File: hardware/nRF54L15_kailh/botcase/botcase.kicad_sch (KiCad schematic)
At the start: 144 parts

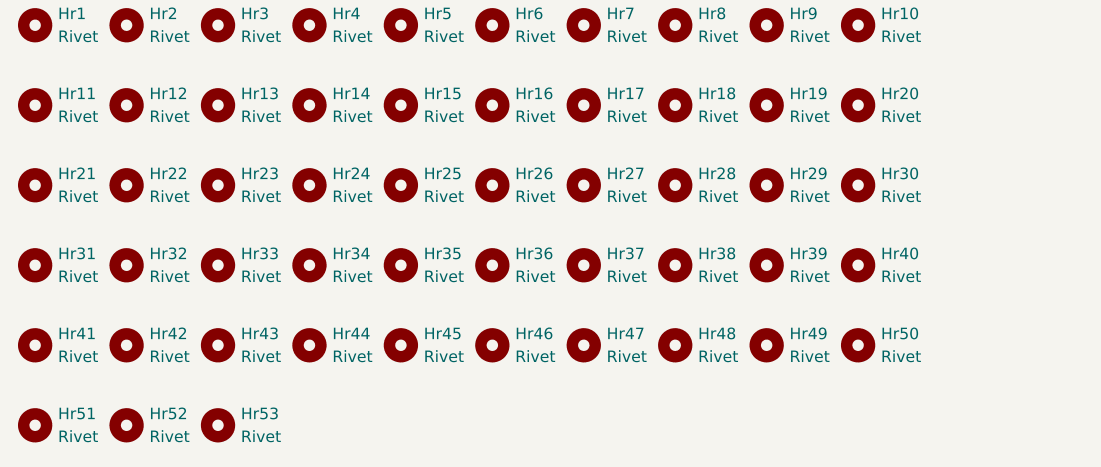
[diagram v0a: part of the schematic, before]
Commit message: M  .gitignore A  hardware/nRF54L15_gateron_kailh_TMR2615/LED.kicad_sch A  hardware/nRF54L15_gateron_kailh_TMR2615/fp-lib-table A  hardware/nRF54L15_gateron_kailh_TMR2615/nRF54L15_gateron_kailh_TMR2615.kicad_pcb A  hardware/nRF54L15_gateron_kailh_TMR2615/nRF54L15_gateron_kailh_TMR2615.kicad_prl A  hardware/nRF54L15_gateron_kailh_TMR2615/nRF54L15_gateron_kailh_TMR2615.kicad_pro A  hardware/nRF54L15_gateron_kailh_TMR2615/nRF54L15_gateron_kailh_TMR2615.kicad_sch A  hardware/nRF54L15_gateron_kailh_TMR2615/pcb-eagle-import.kicad_sym A  hardware/nRF54L15_gateron_kailh_TMR2615/switch.kicad_sch A  hardware/nRF54L15_gateron_kailh_TMR2615/sym-lib-table M  hardware/nRF54L15_kailh/border.py A  hardware/nRF54L15_kailh/botcase/botcase-Edge_Cuts.pdf M  hardware/nRF54L15_kailh/botcase/botcase.kicad_pcb M  hardware/nRF54L15_kailh/botcase/botcase.kicad_sch M  hardware/nRF54L15_kailh/botcover/botcover.kicad_pcb M  hardware/nRF54L15_kailh/botcover/botcover.kicad_sch M  hardware/nRF54L15_kailh/placefp.py A  hardware/nRF54L15_kailh/rebuild_board.py A  hardware/nRF54L15_kailh/run.sh M  hardware/nRF54L15_kailh/swplate/swplate.kicad_pcb M  hardware/nRF54L15_kailh/swplate/swplate.kicad_sch A  hardware/nRF54L15_kailh/tmr-footprints/Kailh_gateron_sw_lowpro.kicad_mod M  hardware/nRF54L15_kailh/tmr-footprints/Kailh_sw_lowpro.kicad_mod A  hardware/nRF54L15_kailh/tmr-footprints/M1.4_tap.kicad_mod A  hardware/nRF54L15_kailh/tmr-footprints/M2.5_tap.kicad_mod A  hardware/nRF54L15_kailh/tmr-footprints/MountingHole_1.6mm_M1.4_NoPad.kicad_mod M  hardware/nRF54L15_kailh/topcase/topcase.kicad_pcb A  hardware/nRF54L15_kailh/wristrest/fp-lib-table A  hardware/nRF54L15_kailh/wristrest/sym-lib-table A  hardware/nRF54L15_kailh/wristrest/wristrest.kicad_pcb A  hardware/nRF54L15_kailh/wristrest/wristrest.kicad_prl A  hardware/nRF54L15_kailh/wristrest/wristrest.kicad_pro A  hardware/nRF54L15_kailh/wristrest/wristrest.kicad_sch
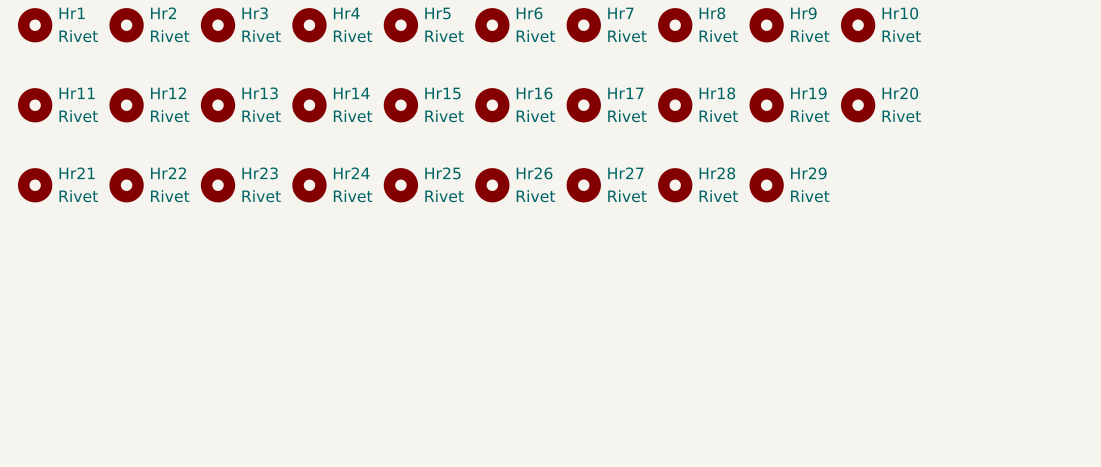
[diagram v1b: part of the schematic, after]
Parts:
- removed Hr30, Hr31, Hr32, Hr33, Hr34, Hr35, Hr36, Hr37, Hr38, Hr39, Hr40, Hr41, Hr42, Hr43, Hr44, Hr45, Hr46, Hr47, Hr48, Hr49, Hr50, Hr51, Hr52, Hr53: Rivet, tmr-lib:RivetInterferenceHole_1.3mm_drill_to_1.35mm, symbol Mechanical:MountingHole
- H1, H10, H11, H12, H13, H14, H15, H16, H2, H3, H4, H5, H6, H7, H8, H9: footprint tmr-lib:PilotHole_2.05mm_M2.5_tap -> tmr-lib:M2.5_tap
- Hr1, Hr10, Hr11, Hr12, Hr13, Hr14, Hr15, Hr16, Hr17, Hr18, Hr19, Hr2, Hr20, Hr21, Hr22, Hr23, Hr24, Hr25, Hr26, Hr27, Hr28, Hr29, Hr3, Hr4, Hr5, Hr6, Hr7, Hr8, Hr9: footprint tmr-lib:RivetInterferenceHole_1.3mm_drill_to_1.35mm -> tmr-lib:M1.4_tap
